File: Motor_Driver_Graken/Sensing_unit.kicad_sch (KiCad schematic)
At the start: 96 parts, among them U20 AMC1300BDWV, U21 AMC1300BDWV, U22 AMC1300BDWV, U23 TL431DBZ, U24 TLV9002IDDFR, U25 TLV9064, U26 AMC1311BDWV, U27 AMC1311BDWV

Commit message: Schematic Changes
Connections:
- net DC_R_+: now also R105.1; no longer R104.1
- net DC_R_-: now also R104.1; no longer R105.1
- net M_T_+: now also R111.2; no longer R110.2
- net M_T_-: now also R110.2; no longer R111.2

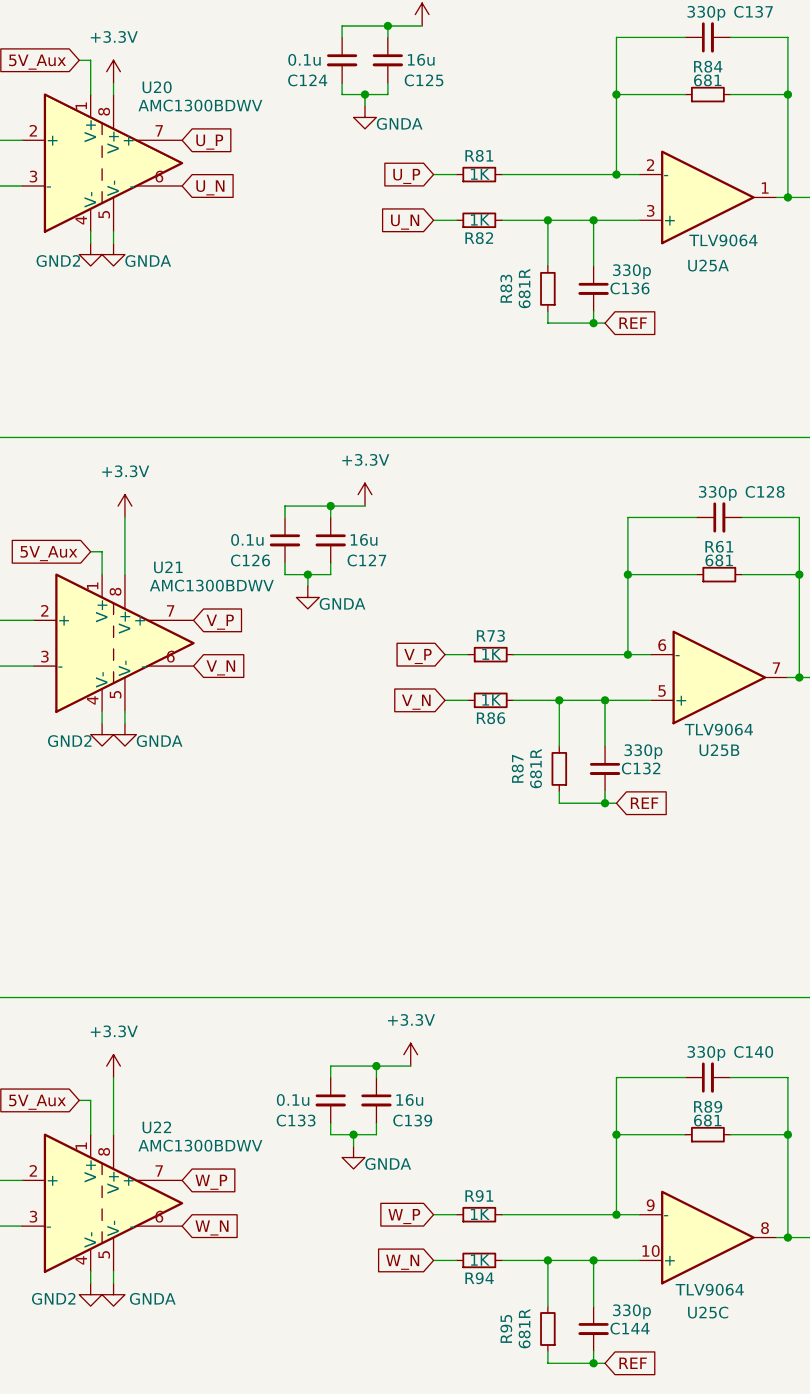
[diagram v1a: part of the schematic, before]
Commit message: Break Resistor Section
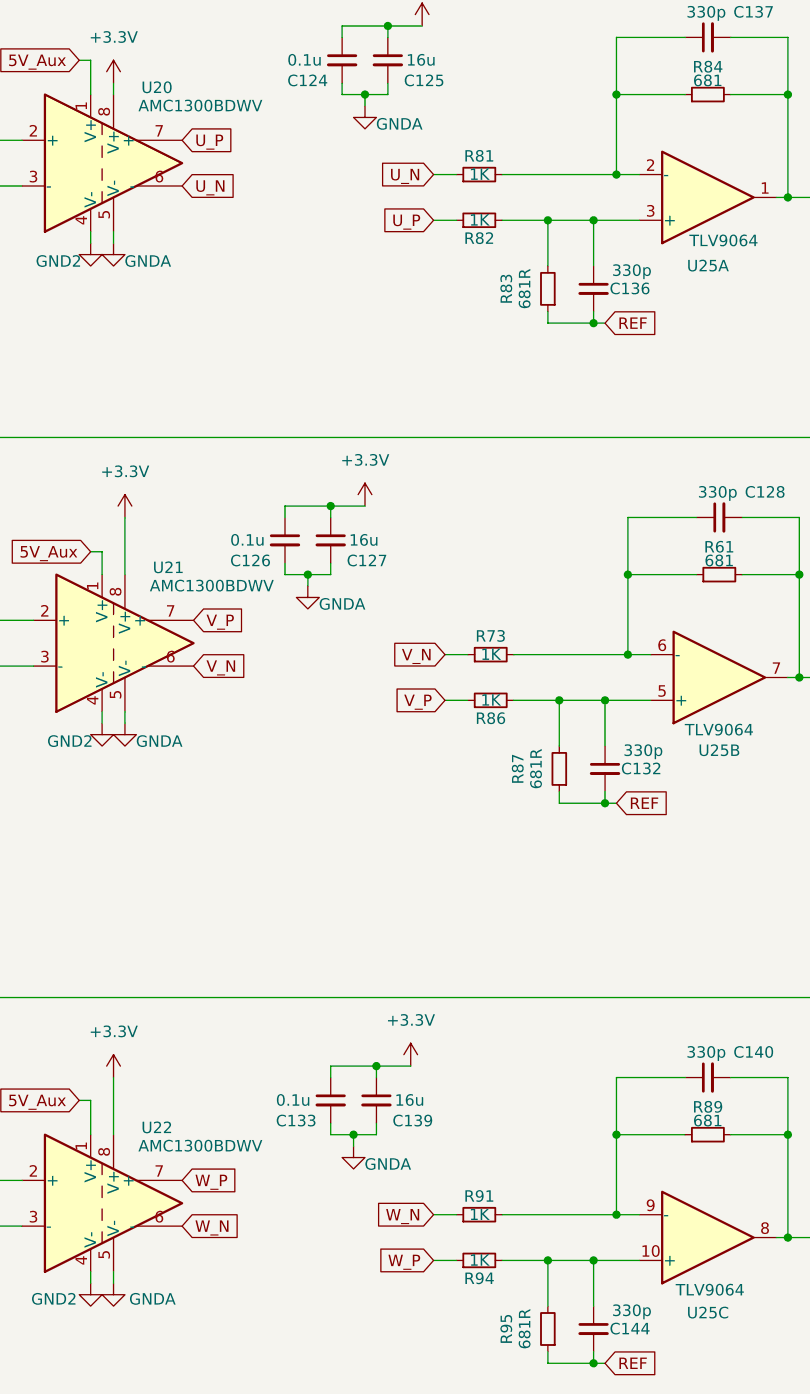
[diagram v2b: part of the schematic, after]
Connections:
- net U_N: now also R81.1; no longer R82.1
- net U_P: now also R82.1; no longer R81.1
- net V_N: now also R73.1; no longer R86.1
- net V_P: now also R86.1; no longer R73.1
- net W_N: now also R91.1; no longer R94.1
- net W_P: now also R94.1; no longer R91.1
